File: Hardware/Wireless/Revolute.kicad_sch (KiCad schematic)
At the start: 55 parts, among them U1 BQ27441-G1, U2 Button, U2 nrf52833_qfn40, U3 AS5600, U4 MIC5504, U5 BQ24075RGT, U7 Conn_01x14_Socket, X1 32.768 kHz, X2 32MHZ

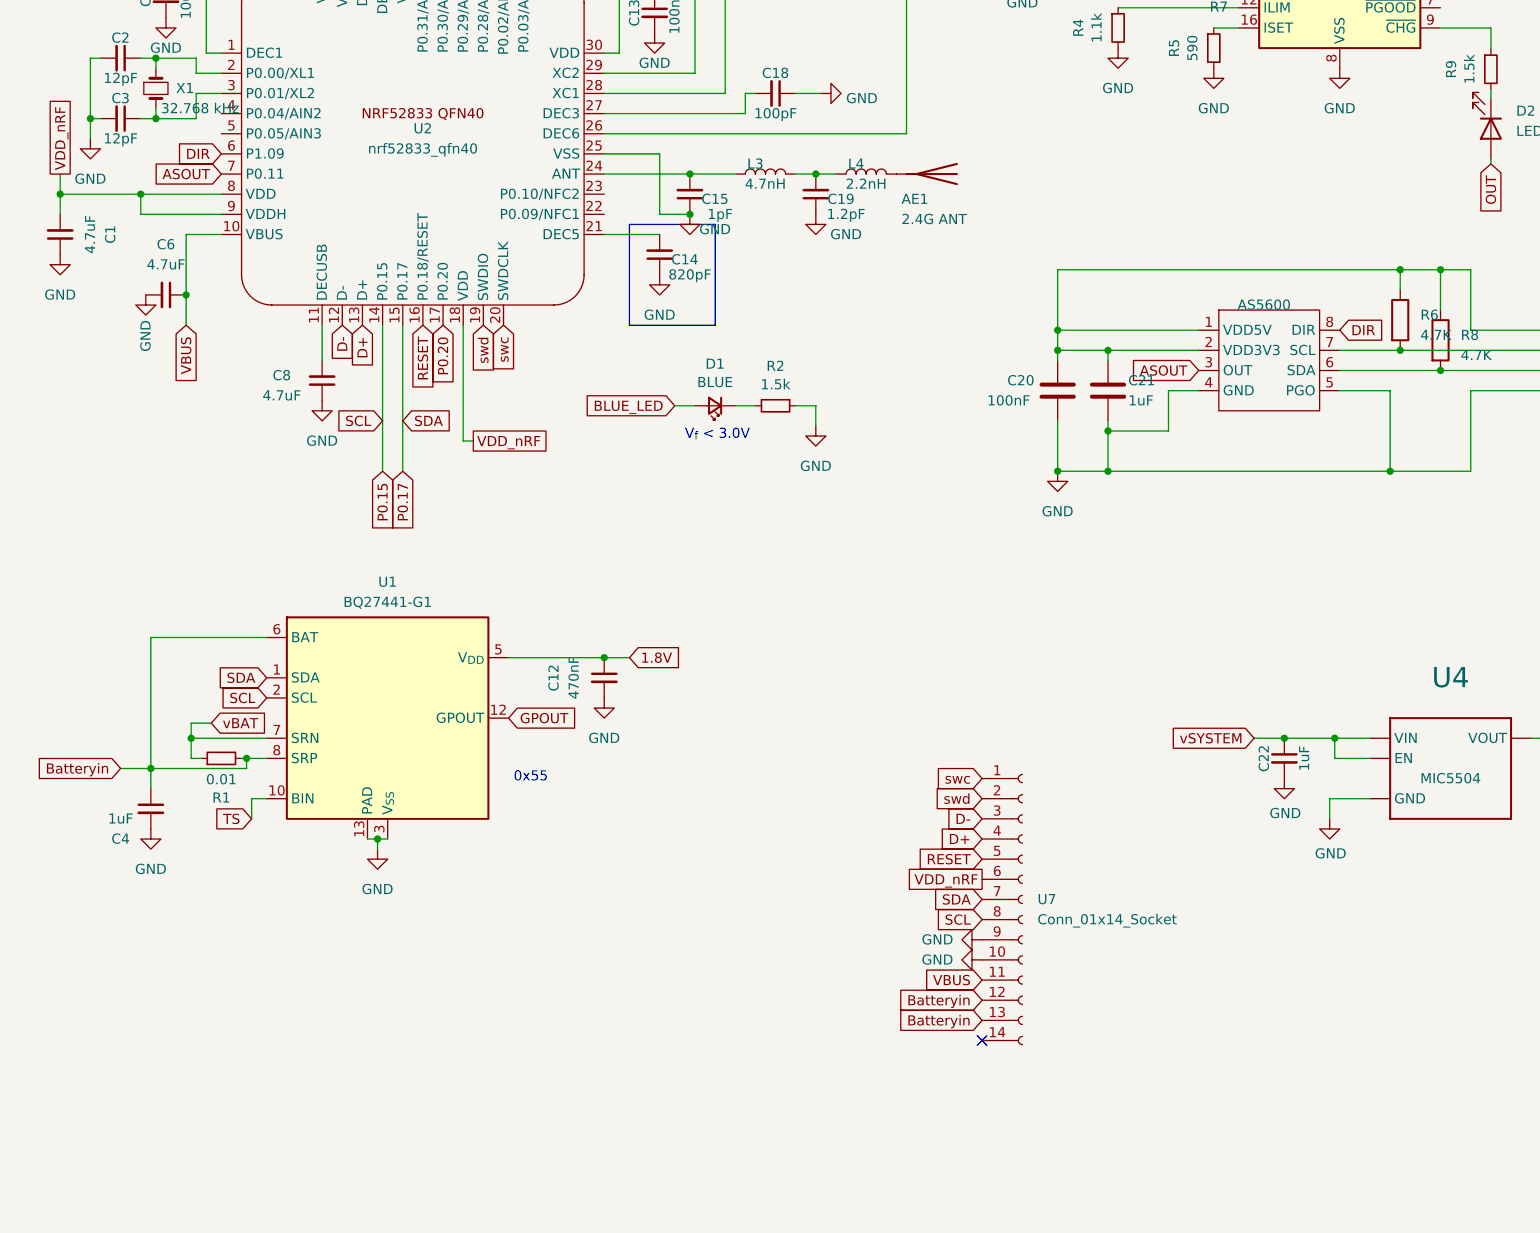
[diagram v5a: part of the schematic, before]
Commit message: added gyro, flex pcb antenna
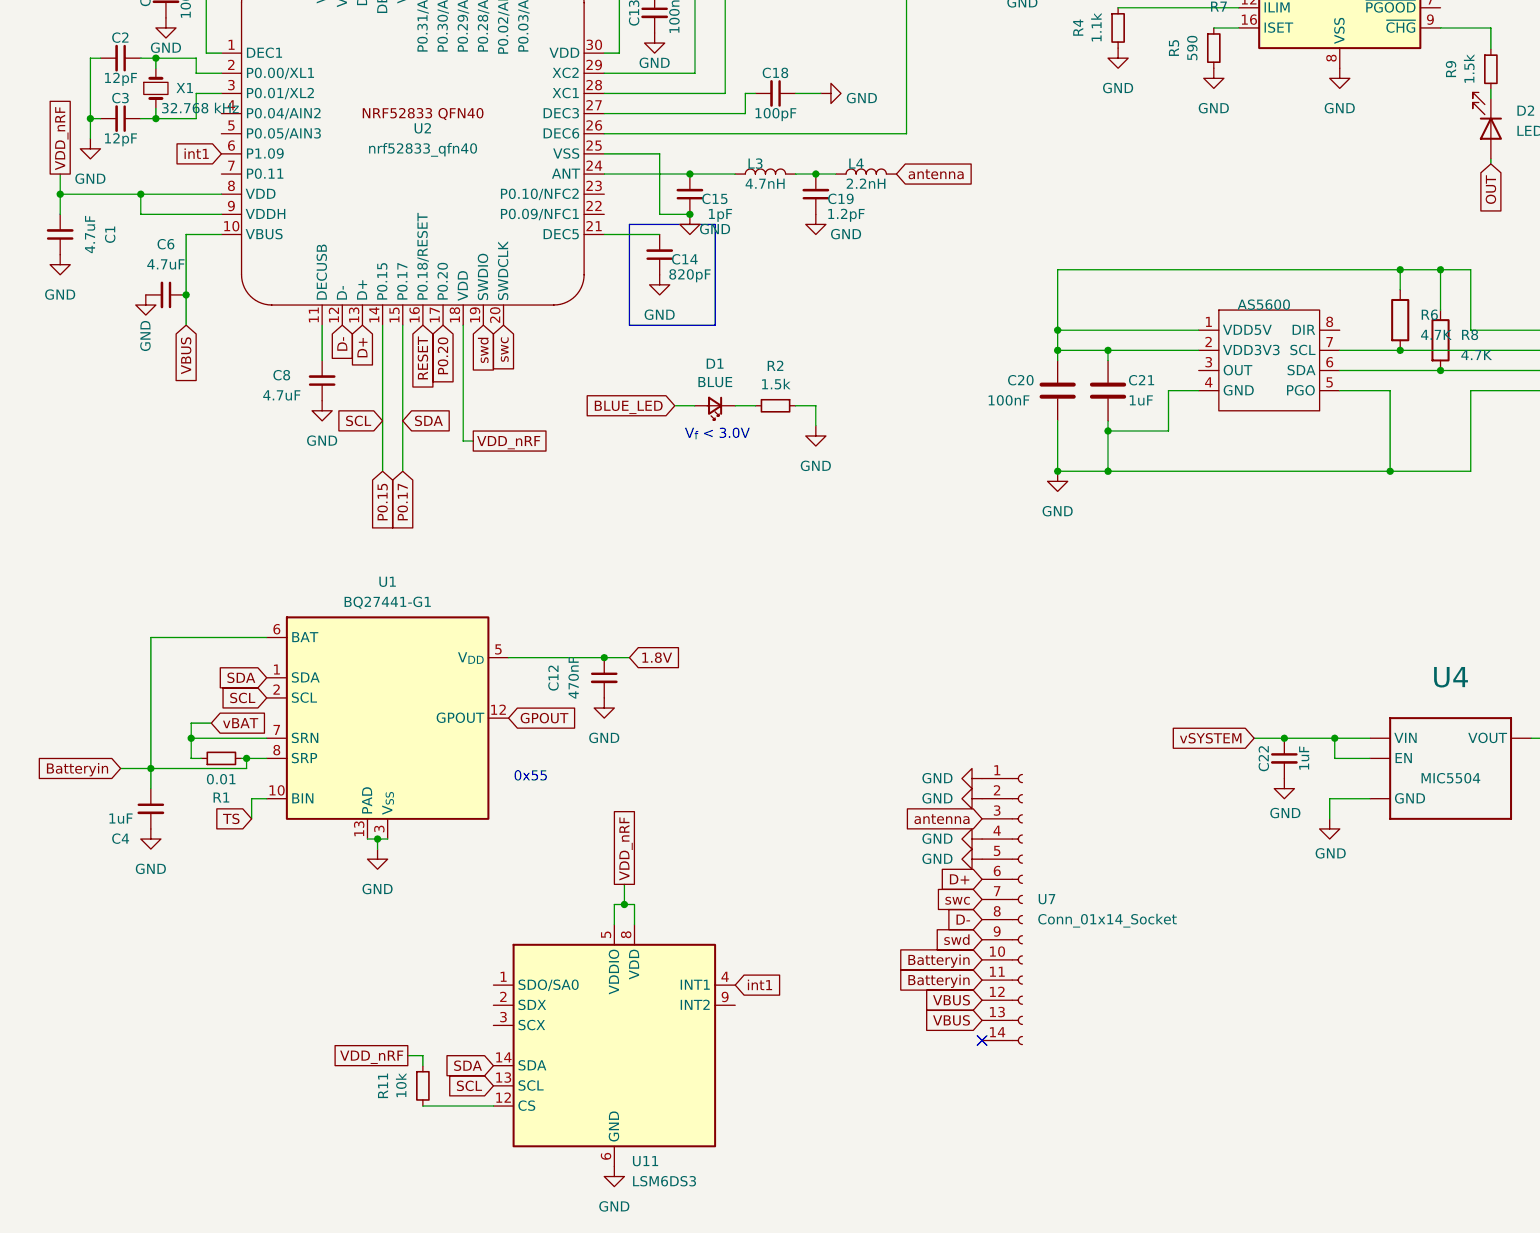
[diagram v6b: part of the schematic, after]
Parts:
- removed AE1: 2.4G ANT, Library:Antenna 2450AT42A100, symbol Device:Antenna
- added R11: 10k, Library:Resistor-0201, symbol Device:R_Small
- added U11: LSM6DS3, Package_LGA:LGA-14_3x2.5mm_P0.5mm_LayoutBorder3x4y, symbol Sensor_Motion:LSM6DS3
- C15, C19: footprint Library:Capacitor-0201 -> Library:Capacitor_0402_1005M-nosilk
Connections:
- net Batteryin: now also U7.10 (Pin_10), U7.11 (Pin_11); no longer U7.12 (Pin_12), U7.13 (Pin_13)
- net D+: now also U7.6 (Pin_6); no longer U7.4 (Pin_4)
- net D-: now also U7.8 (Pin_8); no longer U7.3 (Pin_3)
- net GND: now also U7.1 (Pin_1), U7.2 (Pin_2), U7.4 (Pin_4), U7.5 (Pin_5), U11.6 (GND), U11.7 (GND); no longer U7.10 (Pin_10), U7.9 (Pin_9)
- net P0.15: now also U11.13 (SCL); no longer U7.8 (Pin_8)
- net P0.17: now also U11.14 (SDA); no longer U7.7 (Pin_7)
- net RESET: no longer U7.5 (Pin_5)
- net VBUS: now also U7.12 (Pin_12), U7.13 (Pin_13); no longer U7.11 (Pin_11)
- net VDD_nRF: now also R11.1, U11.5 (VDDIO), U11.8 (VDD); no longer U7.6 (Pin_6)
- net swc: now also U7.7 (Pin_7); no longer U7.1 (Pin_1)
- net swd: now also U7.9 (Pin_9); no longer U7.2 (Pin_2)
- net antenna: now reaches L4.2
- net antenna: now also U7.3 (Pin_3)
- net ASOUT: no longer names the net of U2.7 (P0.11)
- net ASOUT: no longer U3.3 (OUT)
- net DIR: no longer names the net of U3.8 (DIR)
- net DIR: no longer U2.6 (P1.09)
- new net: R11.2, U11.12 (CS)
- new net int1: U11.4 (INT1), U2.6 (P1.09)

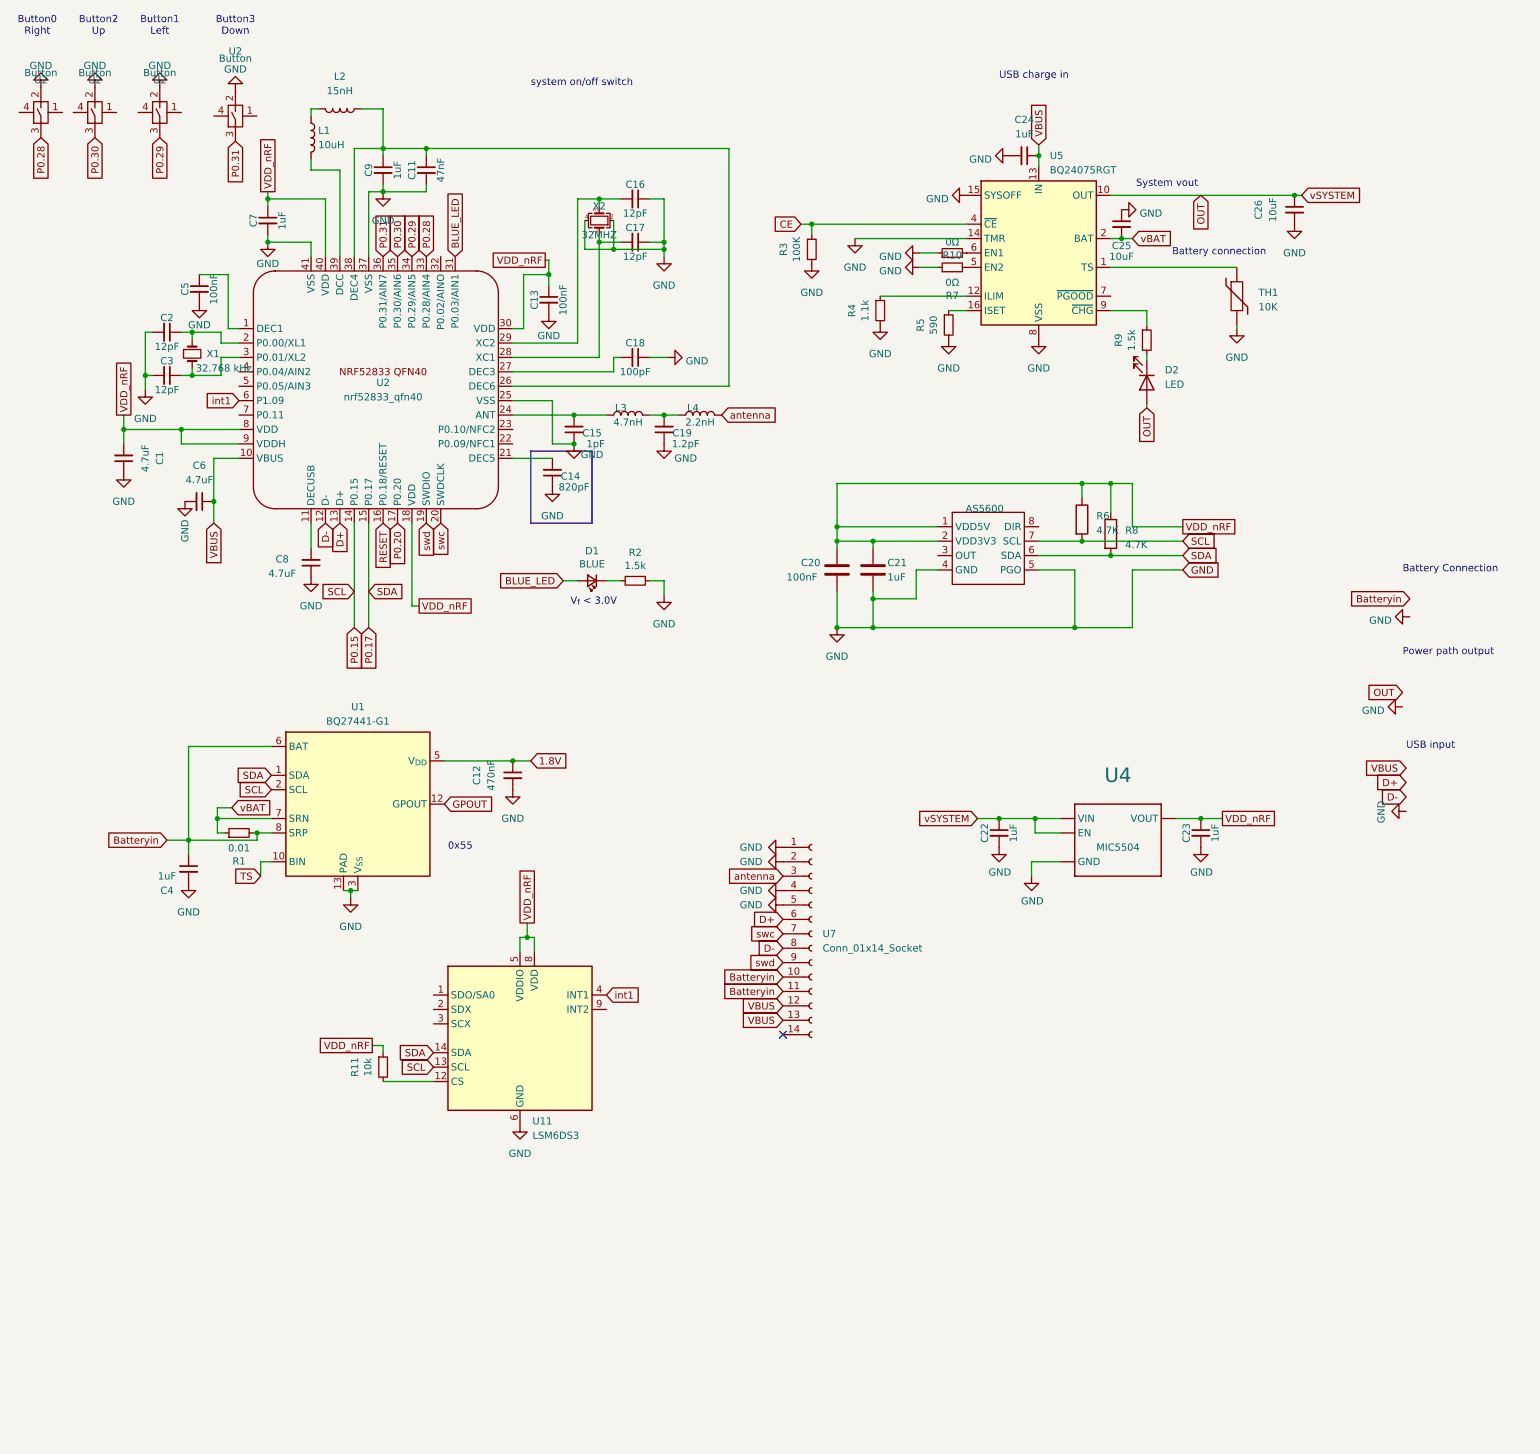
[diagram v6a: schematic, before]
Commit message: revision 3, added mosfets for sensor power cutoff
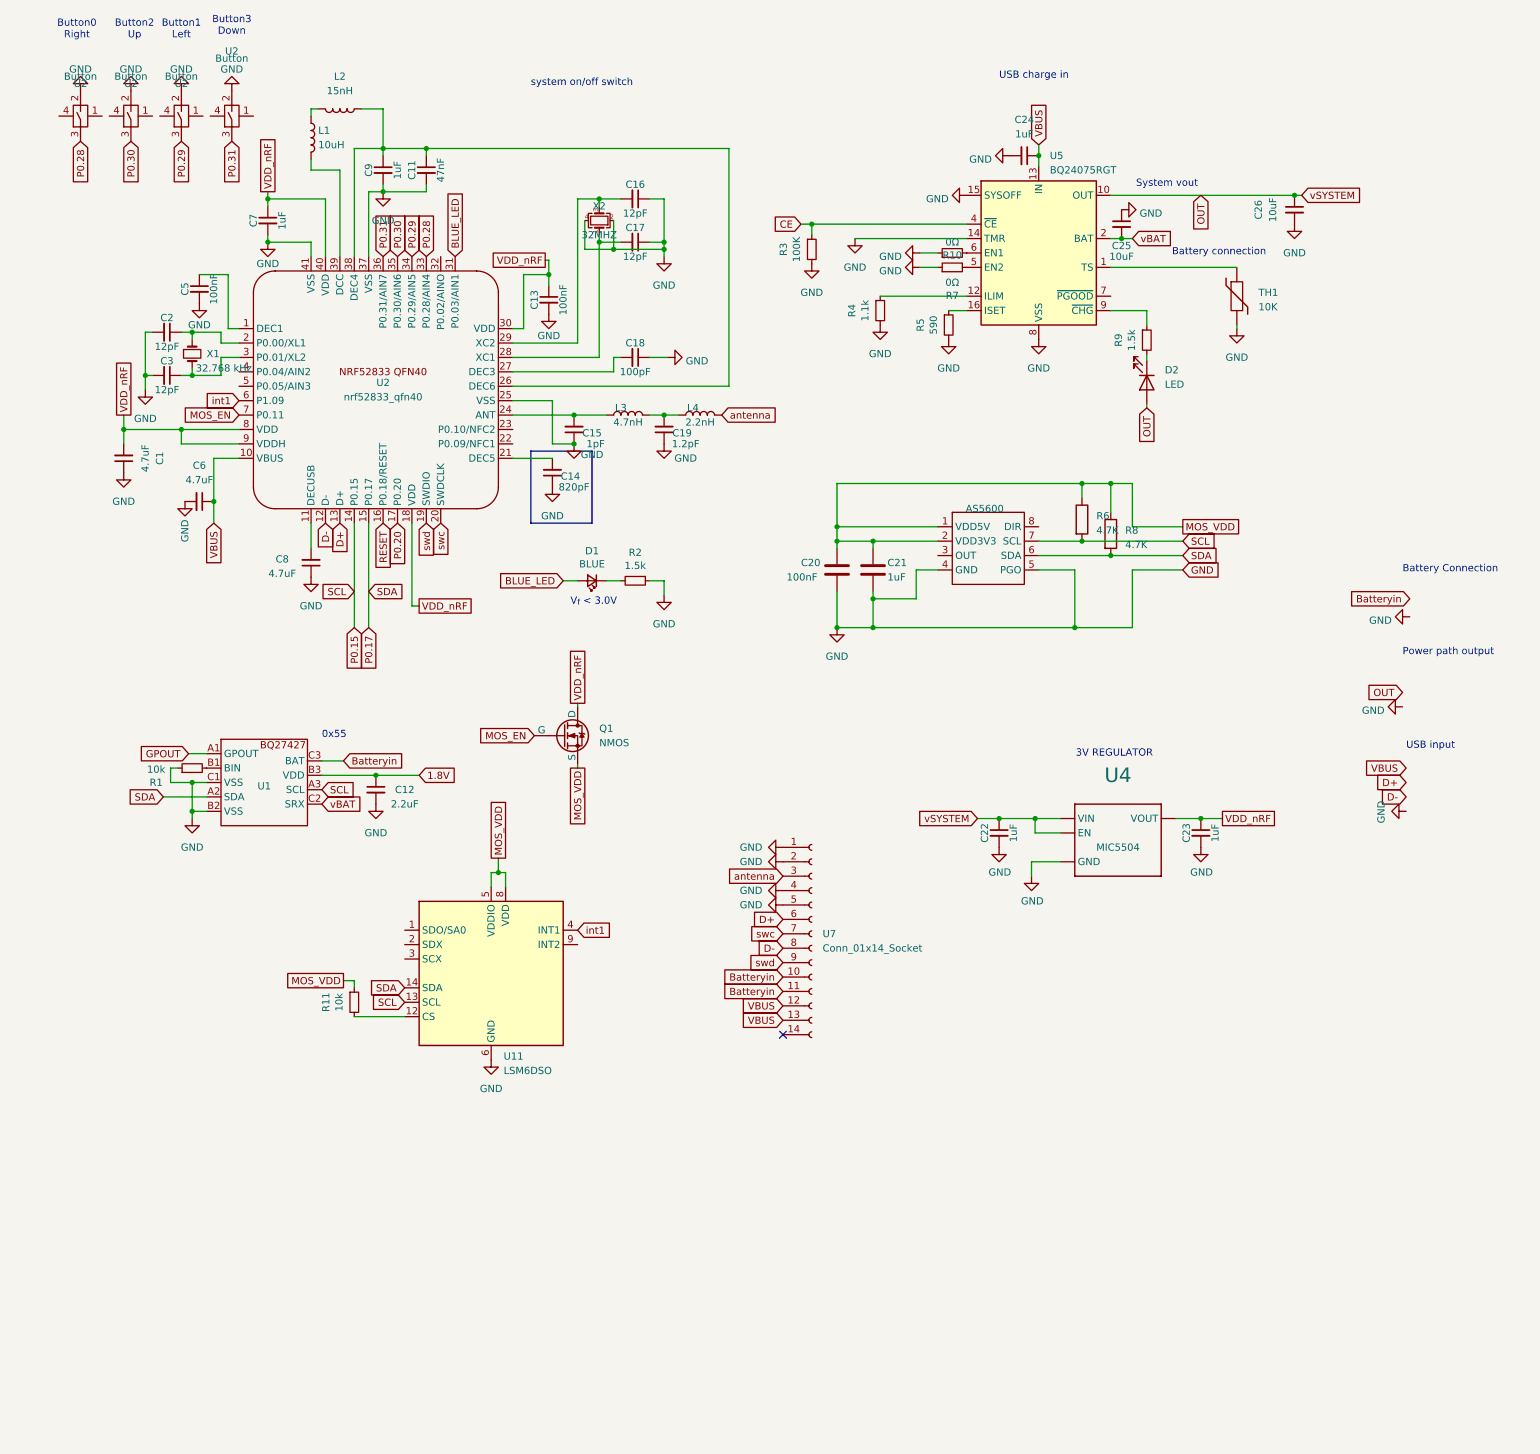
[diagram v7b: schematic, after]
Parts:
- removed C4: 1uF, Library:Capacitor-0201, symbol Device:C_Small
- removed U1: BQ27441-G1, Package_SON:Texas_S-PDSO-N12, symbol Battery_Management:BQ27441-G1
- added Q1: NMOS, Library:Mosfet0402, symbol Simulation_SPICE:NMOS
- added U1: ~, Package_BGA:Texas_DSBGA-9_1.62mmx1.58mm_Layout3x3_P0.5mm, symbol Library:BQ27427
- C12: value 470nF -> 2.2uF; ID 12 -> (none)
- R1: value 0.01 -> 10k; footprint Resistor_SMD:R_0603_1608Metric -> Library:Resistor-0201
- U11: value LSM6DS3 -> LSM6DSO
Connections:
- net 1.8V: now also U1.B3 (VDD)
- net Batteryin: now also U1.C3 (BAT); no longer R1.2
- net GND: now also R1.1, U1.B2 (VSS), U1.C1 (VSS)
- net GPOUT: now also U1.A1 (GPOUT)
- net P0.15: now also U1.A3 (SCL)
- net P0.17: now also U1.A2 (SDA)
- net VDD_nRF: now also Q1.3 (D); no longer C20.1, C21.1, R11.1, R6.1, R8.1, U11.5 (VDDIO), U11.8 (VDD), U3.1 (VDD5V), U3.2 (VDD3V3)
- net vBAT: now also U1.C2 (SRX); no longer R1.1
- net MOS_EN: now reaches U2.7 (P0.11)
- net MOS_EN: now also Q1.1 (G)
- new net: R1.2, U1.B1 (BIN)
- new net MOS_VDD: C20.1, C21.1, Q1.2 (S), R11.1, R6.1, R8.1, U11.5 (VDDIO), U11.8 (VDD), U3.1 (VDD5V), U3.2 (VDD3V3)
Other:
- note added: "3V REGULATOR"
- moved on the sheet: C12, R1, R11, U11, U2
